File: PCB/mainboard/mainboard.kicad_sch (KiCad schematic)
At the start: 65 parts, among them IC1 STM32H743ZIT6, IC2 74HCT125T14-13, IC3 SP4065-08ATG, IC4 SP4065-08ATG, J1 Conn_01x02_right, J10 Uart Connector to pi5, J11 Conn_02x05_Counter_Clockwise, J2 Conn_01x02_left, J3 Conn_01x08_Pin_left, J4 01x06_Pin_LED_Strip_left, J5 01x06_Pin_LED_Strip_right, J6 Conn_01x08_Pin_TOF, J7 Conn_02x03_Counter_Clockwise, J8 Conn_01x08_Pin_right

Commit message: Made the Mainboard BCP Part Layout
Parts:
- removed AC1: LSM6DSOTR, lib:LSM6DS3USTR, symbol LSM6DSOTR:LSM6DSOTR
- removed D5, D6: LED_Geen, lib:LEDC1608X70N, symbol Device:LED
- removed FL1: BLM31KN601SH1L, lib:BLM31KN102BH1L, symbol BLM31KN601SH1L:BLM31KN601SH1L
- removed IC1: STM32H743ZIT6, lib:QFP50P2200X2200X160-144N, symbol STM32H743ZIT6:STM32H743ZIT6
- removed IC2: 74HCT125T14-13, lib:SOP65P640X120-14N, symbol 74HCT125T14-13:74HCT125T14-13
- removed IC3, IC4: SP4065-08ATG, lib:SOP50P488X110-10N, symbol SP4065-08ATG:SP4065-08ATG
- removed J7: Conn_02x03_Counter_Clockwise, symbol Connector_Generic:Conn_02x03_Counter_Clockwise
- removed R10: 270R, Resistor_SMD:R_0201_0603Metric_Pad0.64x0.40mm_HandSolder, symbol Device:R
- removed R9: 100R, Resistor_SMD:R_0201_0603Metric_Pad0.64x0.40mm_HandSolder, symbol Device:R
- added AC2: LSM6DSOTR, lib:LSM6DS3USTR, symbol LSM6DSOTR:LSM6DSOTR
- added IC1: 74HCT125T14-13, lib:SOP65P640X120-14N, symbol 74HCT125T14-13:74HCT125T14-13
- added IC2: SP4065-08ATG, lib:SOP50P488X110-10N, symbol SP4065-08ATG:SP4065-08ATG
- added IC4: STM32H743ZIT6, lib:QFP50P2200X2200X160-144N, symbol STM32H743ZIT6:STM32H743ZIT6
- added J7: TST-105-01-L-D, lib:TST-105-XX-Y-D, symbol TST-105-01-L-D:TST-105-01-L-D
- J1: value Conn_01x02_right -> Right Strip Power
- J2: value Conn_01x02_left -> Left Strip Power
- J3: value Conn_01x08_Pin_left -> Left Strip
- J4: value 01x06_Pin_LED_Strip_left -> LED Strip left
- J5: value 01x06_Pin_LED_Strip_right -> LED Strip right
- J6: value Conn_01x08_Pin_TOF -> Time Of Flight
- J8: value Conn_01x08_Pin_right -> Right Strip
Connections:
- net +3V3: now also AC2.12 (CS), AC2.5 (VDDIO), AC2.8 (VDD), J7.1
- net +5V: now also IC1.10 (3~{OE}), IC1.13 (4~{OE}), IC1.14 (VCC)
- net Battery Voltage: now also IC4.13 (PF3)
- net Boot0: now also IC4.138 (BOOT0)
- net DIN WS2812B Board 1 3.3V: now also IC1.5 (2A), IC4.100 (PA8)
- net DIN WS2812B Board 2 3.3V: now also IC1.2 (1A), IC4.101 (PA9)
- net GND: now also AC2.6 (GND_1), AC2.7 (GND_2), IC1.1 (1~{OE}), IC1.4 (2~{OE}), IC1.7 (GND), IC2.6 (GND), IC4.107 (VSS_7), IC4.120 (VSS_8), IC4.130 (VSS_9), IC4.16 (VSS_1), IC4.38 (VSS_2), IC4.51 (VSS_3), IC4.61 (VSS_4), IC4.83 (VSS_5), IC4.94 (VSS_6), J7.3, J7.5, J7.9
- net GNDA: now also IC4.31 (VSSA)
- net GPIO 1: now also IC4.87 (PG2)
- net GPIO Expansion 1: now also IC2.4 (I/O_4), IC4.141 (PE0)
- net GPIO Expansion 2: now also IC2.3 (I/O_3), IC4.142 (PE1)
- net GPIO Expansion 3: now also IC2.2 (I/O_2), IC4.2 (PE3)
- net NRST: now also IC4.25 (NRST), J7.10
- net PC14-OSC32_IN: now also IC4.8 (PC14-OSC32_IN)
- net PC15-OSC32_OUT: now also IC4.9 (PC15-OSC32_OUT)
- net PDR_ON: now also IC4.143 (PDR_ON)
- net PE2 (LED): now also IC4.1 (PE2)
- net PH0-OSC_IN: now also IC4.23 (PH0-OSC_IN)
- net PH1-OSC_OUT: now also IC4.24 (PH1-OSC_OUT)
- net RX: now also IC4.137 (PB7)
- net SCL: now also AC2.13 (SCL), IC2.8 (I/O_6), IC4.139 (PB8)
- net SDA: now also AC2.14 (SDA), IC2.9 (I/O_7), IC4.140 (PB9)
- net SWCLK: now also IC4.109 (PA14), J7.4
- net SWDIO: now also IC4.105 (PA13), J7.2
- net TX: now also IC4.136 (PB6)
- net VBAT: now also IC4.6 (VBAT)
- net VDD33_USB: now also IC4.95 (VDD33USB)
- net VDDA: now also IC4.33 (VDDA)
- net VDD_MCU: now also IC4.108 (VDD_8), IC4.121 (VDD_9), IC4.131 (VDD_10), IC4.144 (VDD_11), IC4.17 (VDD_1), IC4.30 (VDD_2), IC4.39 (VDD_3), IC4.52 (VDD_4), IC4.62 (VDD_5), IC4.72 (VDD_6), IC4.84 (VDD_7)
- net VREFP: now also IC4.32 (VREF+)
- net XSHUT: now also IC2.1 (I/O_1), IC4.86 (PD15)
- net left_A0: now also IC4.73 (PB12)
- net left_A1: now also IC4.74 (PB13)
- net left_A2: now also IC4.75 (PB14)
- net left_ADC INPUT: now also IC4.26 (PC0)
- net left_¬EN: now also IC4.88 (PG3)
- net right_A0: now also IC4.41 (PA5)
- net right_A1: now also IC4.40 (PA4)
- net right_A2: now also IC4.37 (PA3)
- net right_ADC INPUT: now also IC4.34 (PA0)
- net right_¬EN: now also IC4.46 (PB0)
- net at JP1.2 (B), JP6.1 (A): now also AC2.1 (SDO/SA0)
- net at R37.2: now also IC1.3 (1Y)
- net at R38.2: now also IC1.6 (2Y)
- net PF10 (LED) renamed PE4 (LED)
- net PE4 (LED): now also IC4.3 (PE4)
- new net SWO: IC4.133 (PB3), J7.6
- new net User Button: IC4.79 (PD10)
- new net VCAP_1: IC4.71 (VCAP_1)
- new net VCAP_2: IC4.106 (VCAP_2)
- no-connect marks 2 -> 96
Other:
- note added: "Power Flags"
- moved on the sheet: C21, C22, C23, C24, D3, D4, J10, J11, R39, R40, R41, R7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

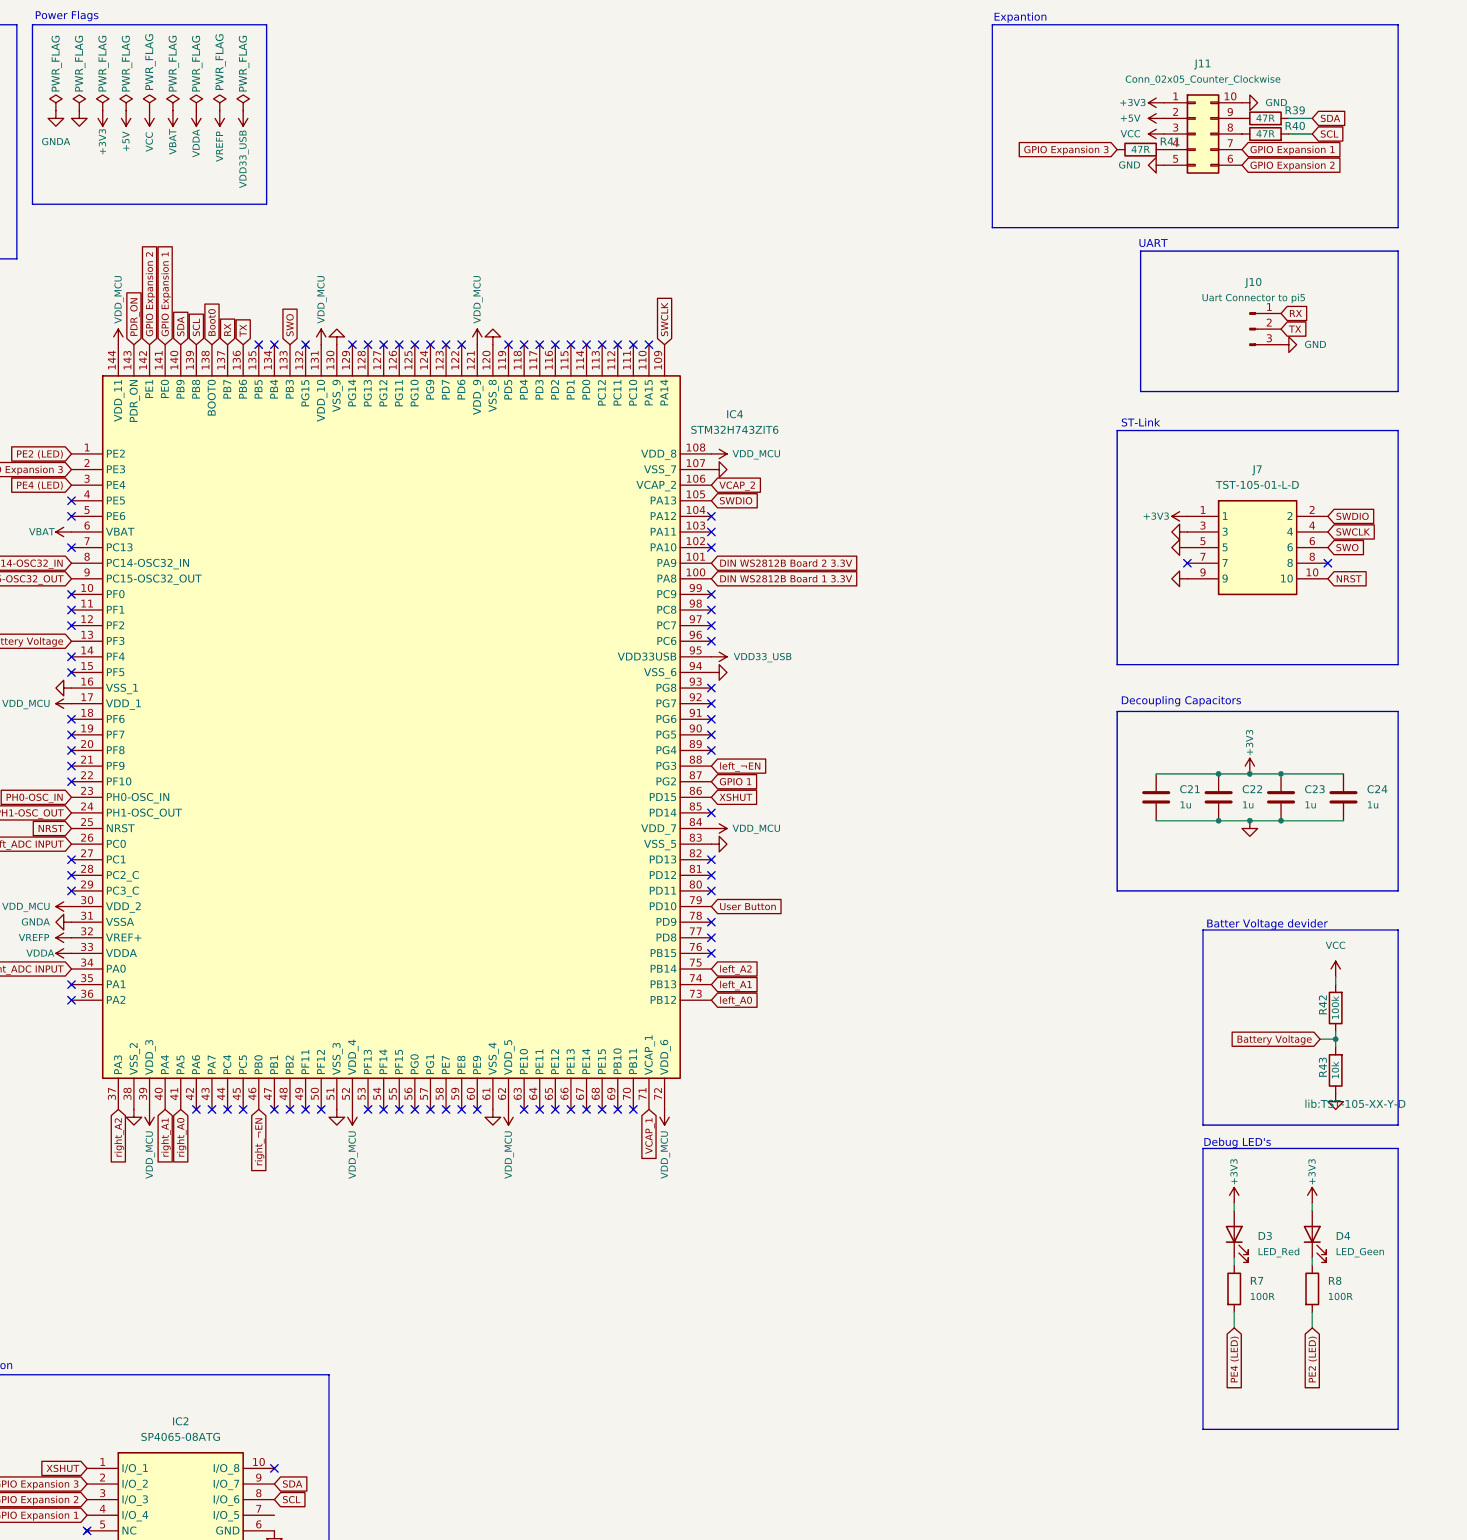
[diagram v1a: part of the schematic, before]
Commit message: Stop tracking renders folder & final Powerstrip and Mainboard PCB
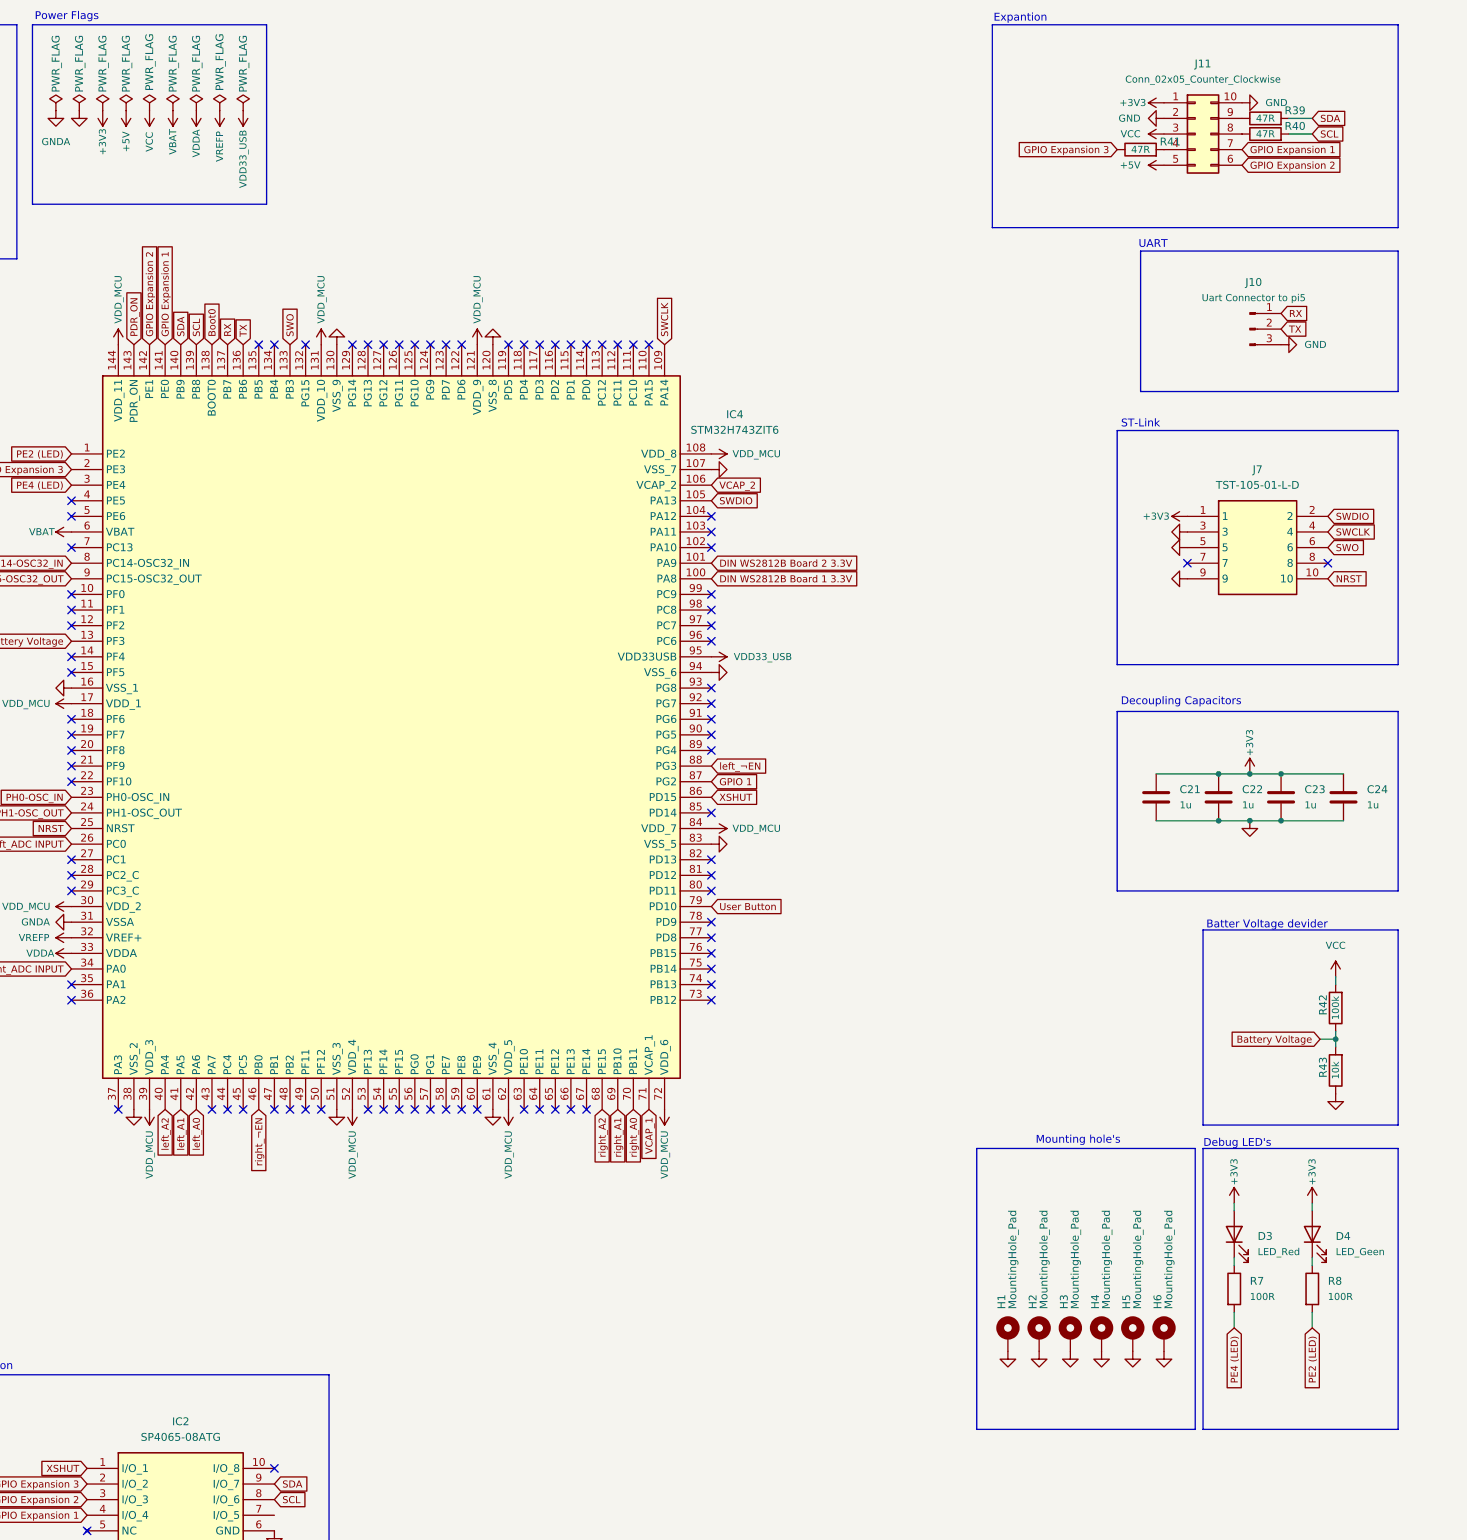
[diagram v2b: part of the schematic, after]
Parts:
- added H1, H2, H3, H4, H5, H6: MountingHole_Pad, MountingHole:MountingHole_3.2mm_M3_Pad_Via, symbol Mechanical:MountingHole_Pad
- J3, J6, J8: footprint Connector_FFC-FPC:Amphenol_F32Q-1A7x1-11008_1x08-1MP_P0.5mm_Horizontal -> lib:17352658
- J4, J5: footprint Connector_FFC-FPC:Amphenol_F32Q-1A7x1-11006_1x06-1MP_P0.5mm_Horizontal -> lib:849526
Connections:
- net +5V: now also J11.5 (Pin_5); no longer J11.2 (Pin_2)
- net GND: now also J11.2 (Pin_2), H1.1, H2.1, H3.1, H4.1, H5.1, H6.1; no longer J11.5 (Pin_5)
- net left_A0: now also IC4.42 (PA6); no longer IC4.73 (PB12)
- net left_A1: now also IC4.41 (PA5); no longer IC4.74 (PB13)
- net left_A2: now also IC4.40 (PA4); no longer IC4.75 (PB14)
- net right_A0: now also IC4.70 (PB11); no longer IC4.41 (PA5)
- net right_A1: now also IC4.69 (PB10); no longer IC4.40 (PA4)
- net right_A2: now also IC4.68 (PE15); no longer IC4.37 (PA3)
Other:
- note added: "Mounting hole's"

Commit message: random upload
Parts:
- removed R39, R40: 47R, Resistor_SMD:R_0201_0603Metric_Pad0.64x0.40mm_HandSolder, symbol Device:R
- R37, R38: value 330R -> 47R
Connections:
- net GND: now also AC2.2 (SDX), AC2.3 (SCX)
- net SCL: now also J11.8 (Pin_8)
- net SDA: now also J11.9 (Pin_9)
- no-connect marks 96 -> 94

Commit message: random
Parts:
- added J9: LED_CAM, Connector_PinHeader_2.54mm:PinHeader_1x02_P2.54mm_Vertical, symbol Connector_Generic:Conn_01x02
- added R39: 100R, Resistor_SMD:R_0201_0603Metric_Pad0.64x0.40mm_HandSolder, symbol Device:R
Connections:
- net +3V3: now also J9.1 (Pin_1)
- net LED_CAM: now reaches IC4.116 (PD2)
- net LED_CAM: now also R39.2
- new net: J9.2 (Pin_2), R39.1
- no-connect marks 94 -> 93
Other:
- moved on the sheet: H1, H2, H3, H4, H5, H6
